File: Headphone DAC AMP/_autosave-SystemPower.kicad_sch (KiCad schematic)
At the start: 34 parts, among them U1 NCV8187AMTW090TAG, U11 ADP5071AREZ-R7, U6 MCP1727-1802xSN, U7 MCP1727-3302xSN

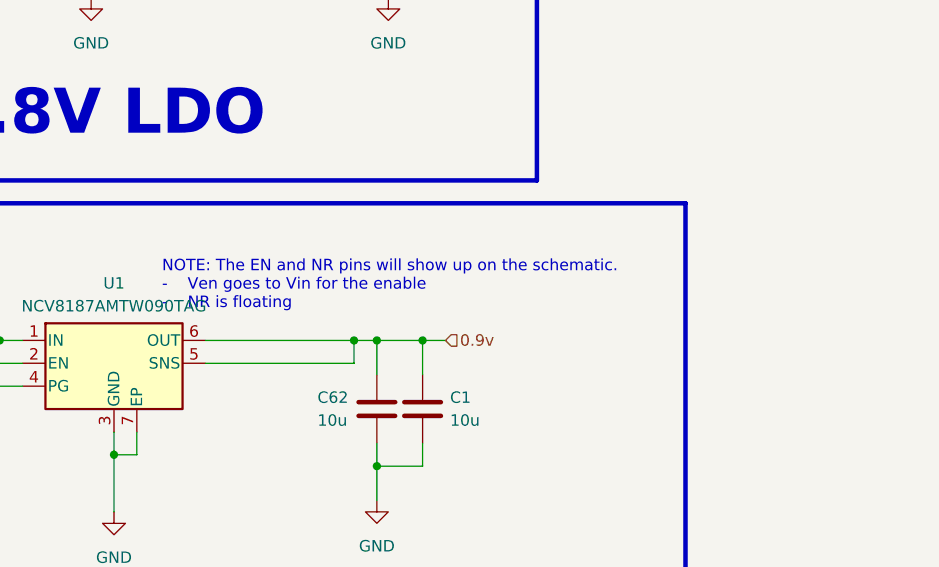
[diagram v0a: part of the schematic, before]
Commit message: Added 0.9V regulator footprint
There is still an issue where the nets are not being populated correctly across the schematic to PCB view
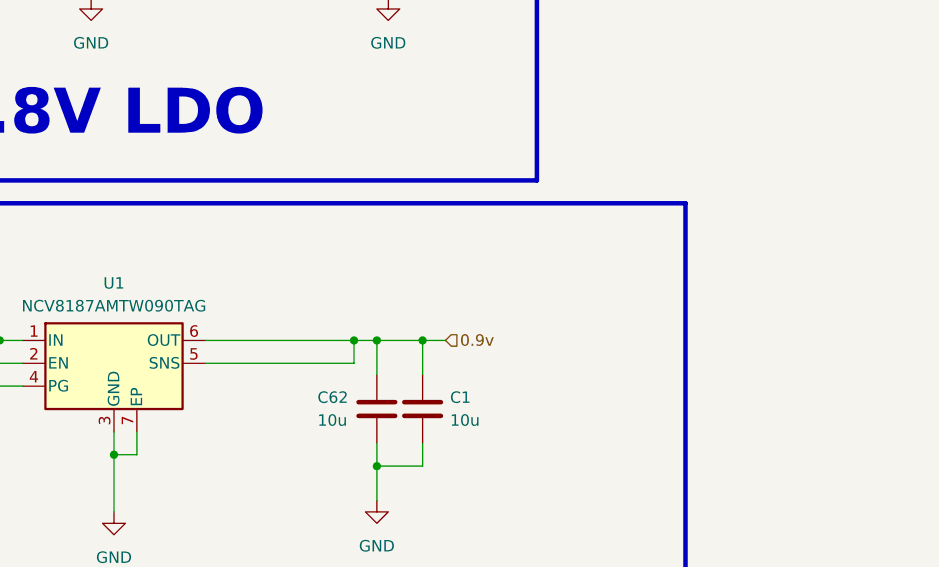
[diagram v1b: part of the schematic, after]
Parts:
- U1: footprint Package_SON:WSON-6-1EP_3x3mm_P0.95mm -> NCV8187AMTW090TAG:SON65P200X200X80-7N
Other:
- note removed: "NOTE: The EN and NR pins will show up on the schematic. - Ven goes to Vin for the enable - NR is floating"
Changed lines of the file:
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@@
 		)
 	)
-	(text "NOTE: The EN and NR pins will show up on the schematic.\n-	Ven goes to Vin for the enable\n-	NR is floating"
-		(exclude_from_sim no)
-		(at 77.724 142.494 0)
-		(effects
-			(font
-				(size 1.27 1.27)
-			)
-			(justify left)
-		)
-	)
 	(text "1.8V LDO"
 		(exclude_from_sim no)
@@
 			)
 		)
-		(property "Footprint" "Package_SON:WSON-6-1EP_3x3mm_P0.95mm"
+		(property "Footprint" "NCV8187AMTW090TAG:SON65P200X200X80-7N"
 			(at 72.39 151.13 0)
 			(effects
